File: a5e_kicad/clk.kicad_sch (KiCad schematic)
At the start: 11 parts, among them Y2 ASV-xxxMHz

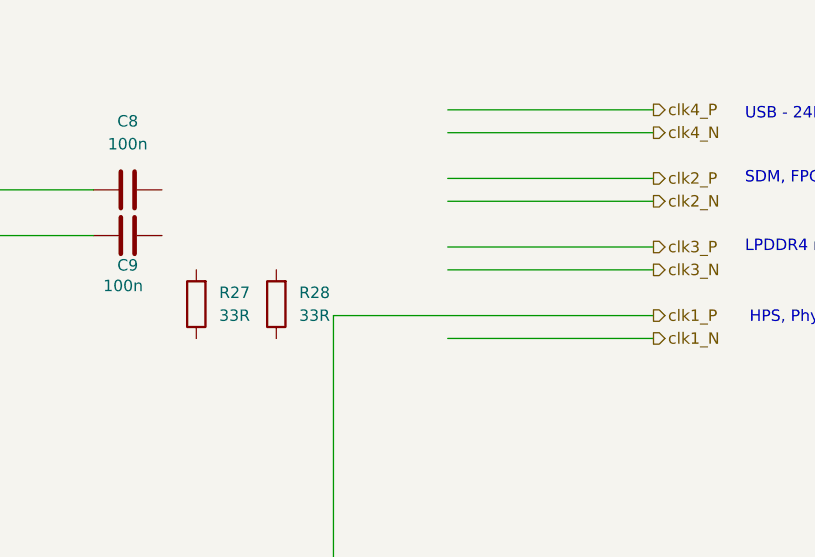
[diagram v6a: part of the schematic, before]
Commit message: add ac biasing to lpddr ref clock
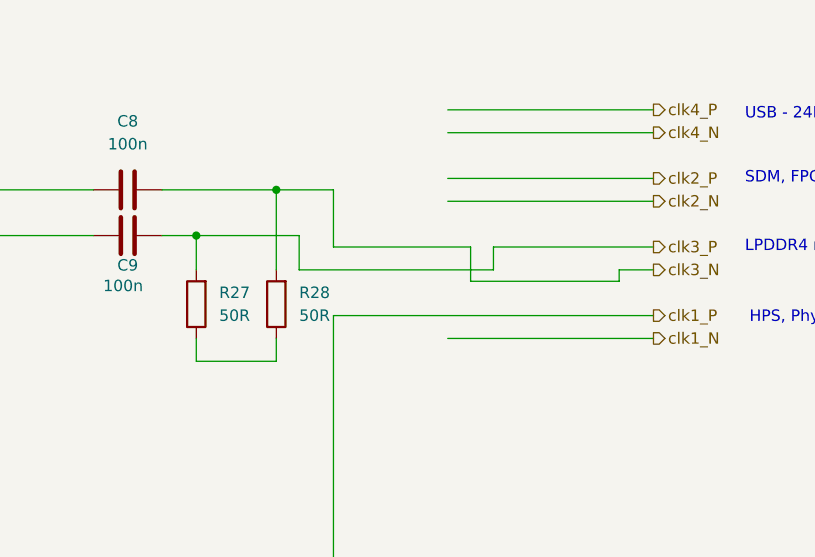
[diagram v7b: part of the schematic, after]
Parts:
- C8, C9, R25: footprint (none) -> Capacitor_SMD:C_0402_1005Metric
- R26: footprint (none) -> Resistor_SMD:R_0402_1005Metric
- R27, R28: value 33R -> 50R; footprint (none) -> Resistor_SMD:R_0402_1005Metric
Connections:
- net clk3_N: now also C8.2, R28.2
- net clk3_P: now also C9.2, R27.2
- net at R27.1: now also R28.1
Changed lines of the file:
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@@
+	)
+	(junction
+		(at 147.32 59.69)
+		(diameter 0)
+		(color 0 0 0 0)
 	)
 	(junction
@@
 	)
 	(junction
+		(at 156.21 54.61)
+		(diameter 0)
+		(color 0 0 0 0)
+	)
+	(junction
 		(at 107.95 100.33)
 		(diameter 0)
@@
 	(wire
 		(pts
-			(xy 175.26 63.5) (xy 198.12 63.5)
-		)
-		(stroke
-			(width 0)
-			(type default)
-		)
-	)
-	(wire
-		(pts
 			(xy 175.26 55.88) (xy 198.12 55.88)
 		)
@@
 	(wire
 		(pts
+			(xy 162.56 54.61) (xy 162.56 60.96)
+		)
+		(stroke
+			(width 0)
+			(type default)
+		)
+	)
+	(wire
+		(pts
+			(xy 158.75 59.69) (xy 147.32 59.69)
+		)
+		(stroke
+			(width 0)
+			(type default)
+		)
+	)
+	(wire
+		(pts
 			(xy 95.25 68.58) (xy 95.25 72.39)
 		)
@@
 	(wire
 		(pts
+			(xy 194.31 64.77) (xy 194.31 63.5)
+		)
+		(stroke
+			(width 0)
+			(type default)
+		)
+	)
+	(wire
+		(pts
 			(xy 107.95 116.84) (xy 107.95 118.11)
 		)
@@
 	(wire
 		(pts
+			(xy 180.34 63.5) (xy 180.34 60.96)
+		)
+		(stroke
+			(width 0)
+			(type default)
+		)
+	)
+	(wire
+		(pts
 			(xy 106.68 54.61) (xy 116.84 54.61)
 		)
@@
 	(wire
 		(pts
+			(xy 156.21 73.66) (xy 156.21 71.12)
+		)
+		(stroke
+			(width 0)
+			(type default)
+		)
+	)
+	(wire
+		(pts
 			(xy 63.5 53.34) (xy 63.5 43.18)
 		)
@@
 	(wire
 		(pts
+			(xy 156.21 63.5) (xy 156.21 54.61)
+		)
+		(stroke
+			(width 0)
+			(type default)
+		)
+	)
+	(wire
+		(pts
+			(xy 147.32 71.12) (xy 147.32 73.66)
+		)
+		(stroke
+			(width 0)
+			(type default)
+		)
+	)
+	(wire
+		(pts
 			(xy 106.68 59.69) (xy 116.84 59.69)
 		)
@@
 	(wire
 		(pts
-			(xy 175.26 60.96) (xy 198.12 60.96)
+			(xy 143.51 54.61) (xy 156.21 54.61)
+		)
+		(stroke
+			(width 0)
+			(type default)
+		)
+	)
+	(wire
+		(pts
+			(xy 162.56 60.96) (xy 177.8 60.96)
 		)
 		(stroke
@@
 	(wire
 		(pts
+			(xy 158.75 63.5) (xy 158.75 59.69)
+		)
+		(stroke
+			(width 0)
+			(type default)
+		)
+	)
+	(wire
+		(pts
+			(xy 147.32 73.66) (xy 156.21 73.66)
+		)
+		(stroke
+			(width 0)
+			(type default)
+		)
+	)
+	(wire
+		(pts
 			(xy 95.25 41.91) (xy 95.25 43.18)
 		)
@@
 	(wire
 		(pts
+			(xy 180.34 60.96) (xy 198.12 60.96)
+		)
+		(stroke
+			(width 0)
+			(type default)
+		)
+	)
+	(wire
+		(pts
+			(xy 177.8 64.77) (xy 194.31 64.77)
+		)
+		(stroke
+			(width 0)
+			(type default)
+		)
+	)
+	(wire
+		(pts
 			(xy 95.25 66.04) (xy 95.25 68.58)
 		)
@@
 	(wire
 		(pts
+			(xy 158.75 63.5) (xy 180.34 63.5)
+		)
+		(stroke
+			(width 0)
+			(type default)
+		)
+	)
+	(wire
+		(pts
 			(xy 107.95 118.11) (xy 107.95 119.38)
 		)
@@
 	(wire
 		(pts
+			(xy 156.21 54.61) (xy 162.56 54.61)
+		)
+		(stroke
+			(width 0)
+			(type default)
+		)
+	)
+	(wire
+		(pts
+			(xy 177.8 60.96) (xy 177.8 64.77)
+		)
+		(stroke
+			(width 0)
+			(type default)
+		)
+	)
+	(wire
+		(pts
 			(xy 63.5 43.18) (xy 95.25 43.18)
 		)
@@
 	(wire
 		(pts
+			(xy 147.32 63.5) (xy 147.32 59.69)
+		)
+		(stroke
+			(width 0)
+			(type default)
+		)
+	)
+	(wire
+		(pts
 			(xy 107.95 100.33) (xy 107.95 101.6)
 		)
@@
 	(wire
 		(pts
+			(xy 147.32 59.69) (xy 143.51 59.69)
+		)
+		(stroke
+			(width 0)
+			(type default)
+		)
+	)
+	(wire
+		(pts
 			(xy 81.28 100.33) (xy 93.98 100.33)
+		)
+		(stroke
+			(width 0)
+			(type default)
+		)
+	)
+	(wire
+		(pts
+			(xy 194.31 63.5) (xy 198.12 63.5)
 		)
 		(stroke
@@
 			)
 		)
-		(property "Footprint" ""
+		(property "Footprint" "Capacitor_SMD:C_0402_1005Metric"
 			(at 143.51 58.7248 0)
 			(hide yes)
@@
 			)
 		)
-		(property "Footprint" ""
+		(property "Footprint" "Resistor_SMD:R_0402_1005Metric"
 			(at 120.65 61.468 90)
 			(hide yes)
@@
 		(in_pos_files yes)
 		(dnp no)
-		(fields_autoplaced yes)
 		(property "Reference" "C8"
 			(at 139.7 46.99 90)
@@
 			)
 		)
-		(property "Footprint" ""
+		(property "Footprint" "Capacitor_SMD:C_0402_1005Metric"
 			(at 143.51 53.6448 0)
 			(hide yes)
@@
 			)
 		)
-		(property "Value" "33R"
+		(property "Value" "50R"
 			(at 149.86 68.5799 0)
 			(show_name no)
@@
 			)
 		)
-		(property "Footprint" ""
+		(property "Footprint" "Resistor_SMD:R_0402_1005Metric"
 			(at 149.098 67.31 90)
 			(hide yes)
@@
 			)
 		)
-		(property "Value" "33R"
+		(property "Value" "50R"
 			(at 158.75 68.5799 0)
 			(show_name no)
@@
 			)
 		)
-		(property "Footprint" ""
+		(property "Footprint" "Resistor_SMD:R_0402_1005Metric"
 			(at 157.988 67.31 90)
 			(hide yes)
@@
 			)
 		)
-		(property "Footprint" ""
+		(property "Footprint" "Capacitor_SMD:C_0402_1005Metric"
 			(at 120.65 56.388 90)
 			(hide yes)
